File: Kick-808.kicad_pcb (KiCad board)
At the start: 2 copper layers, 0 parts

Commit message: PCB layout preparation.
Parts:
- added Accent1: AudioJack2_SwitchT, Local:PJ398SM, F.Cu at (197.0, 93.5)
- added C1: 100n, Capacitor_SMD:C_0603_1608Metric, F.Cu at (225.6, 79.8)
- added C10: 15n, Capacitor_SMD:C_0603_1608Metric, F.Cu at (214.2, 91.6)
- added C11: 22n, Capacitor_SMD:C_0603_1608Metric, F.Cu at (208.5, 93.9)
- added C12: 1u, Capacitor_SMD:C_0603_1608Metric, F.Cu at (204.0, 98.5)
- added C13: 10u, Capacitor_SMD:CP_Elec_4x5.8, F.Cu at (217.3, 74.4)
- added C2: 100n, Capacitor_SMD:C_0603_1608Metric, F.Cu at (219.8, 83.1)
- added C3: 22u, Capacitor_SMD:CP_Elec_5x5.4, F.Cu at (207.7, 89.2)
- added C4: 22u, Capacitor_SMD:CP_Elec_5x5.4, F.Cu at (179.0, 105.1)
- added C5: 15n, Capacitor_SMD:C_0603_1608Metric, F.Cu at (225.6, 77.3)
- added C6: 100n, Capacitor_SMD:C_0603_1608Metric, F.Cu at (172.7, 109.8)
- added C7: 100n, Capacitor_SMD:C_0603_1608Metric, F.Cu at (204.0, 101.0)
- added C8: 33n, Capacitor_SMD:C_0603_1608Metric, F.Cu at (216.5, 94.1)
- added C9: 15n, Capacitor_SMD:C_0603_1608Metric, F.Cu at (208.5, 96.4)
- added D1: 1N4148, Diode_SMD:D_SOD-123, F.Cu at (186.4, 109.6)
- added D2: 1N4148, Diode_SMD:D_SOD-123, F.Cu at (224.0, 73.1)
- added D3: 1N4148, Diode_SMD:D_SOD-123, F.Cu at (216.3, 79.0)
- added Decay1: 100k, Local:AlpsRK09K, F.Cu at (167.3, 77.6)
- added FB1: Ferrite_Bead, Inductor_SMD:L_0603_1608Metric, F.Cu at (195.2, 107.1)
- added FB2: Ferrite_Bead, Inductor_SMD:L_0603_1608Metric, F.Cu at (218.6, 86.5)
- added J3: Conn_02x05_Odd_Even, Connector_PinHeader_2.54mm:PinHeader_2x05_P2.54mm_Vertical, F.Cu at (176.9, 89.2)
- added Mod1: 10k, Local:AlpsRK09K, F.Cu at (196.0, 77.6)
- added Mod2: 100k, Local:AlpsRK09K, F.Cu at (181.7, 77.6)
- added Output1: AudioJack2_SwitchT, Local:PJ398SM, F.Cu at (208.3, 78.0)
- added Q1: BC847, Package_TO_SOT_SMD:SOT-23, F.Cu at (204.3, 94.9)
- added Q2: BC847, Package_TO_SOT_SMD:SOT-23, F.Cu at (215.6, 82.9)
- added Q3: BC857, Package_TO_SOT_SMD:SOT-23, F.Cu at (194.7, 103.5)
- added Q4: BC847, Package_TO_SOT_SMD:SOT-23, F.Cu at (214.4, 88.1)
- added Q5: BC847, Package_TO_SOT_SMD:SOT-23, F.Cu at (221.4, 79.6)
- added Q6: BC847, Package_TO_SOT_SMD:SOT-23, F.Cu at (199.1, 103.5)
- added Q7: BC847, Package_TO_SOT_SMD:SOT-23, F.Cu at (229.1, 73.7)
- added R1: 2k2, Resistor_SMD:R_0603_1608Metric, F.Cu at (191.2, 109.2)
- added R10: 10k, Resistor_SMD:R_0603_1608Metric, F.Cu at (203.3, 106.0)
- added R11: 100k, Resistor_SMD:R_0603_1608Metric, F.Cu at (226.2, 90.6)
- added R12: 1M, Resistor_SMD:R_0603_1608Metric, F.Cu at (218.2, 91.6)
- added R13: 4k7, Resistor_SMD:R_0603_1608Metric, F.Cu at (208.0, 98.9)
- added R14: 10k, Resistor_SMD:R_0603_1608Metric, F.Cu at (203.3, 103.5)
- added R15: 22k, Resistor_SMD:R_0603_1608Metric, F.Cu at (229.6, 77.3)
- added R16: 100k, Resistor_SMD:R_0603_1608Metric, F.Cu at (218.6, 89.0)
- added R17: 4k7, Resistor_SMD:R_0603_1608Metric, F.Cu at (225.6, 82.3)
- added R18: 100k, Resistor_SMD:R_0603_1608Metric, F.Cu at (212.5, 94.1)
- added R19: 1M, Resistor_SMD:R_0603_1608Metric, F.Cu at (199.3, 107.1)
- added R2: 1k5, Resistor_SMD:R_0603_1608Metric, F.Cu at (180.8, 109.8)
- added R20: 1M, Resistor_SMD:R_0603_1608Metric, F.Cu at (208.0, 101.4)
- added R21: 1k, Resistor_SMD:R_0603_1608Metric, F.Cu at (176.7, 109.8)
- added R22: 220, Resistor_SMD:R_0603_1608Metric, F.Cu at (216.1, 99.1)
- added R23: 100k, Resistor_SMD:R_0603_1608Metric, F.Cu at (226.7, 87.3)
- added R24: 470k, Resistor_SMD:R_0603_1608Metric, F.Cu at (220.5, 94.1)
- added R25: 10k, Resistor_SMD:R_0603_1608Metric, F.Cu at (216.5, 96.6)
- added R26: 100k, Resistor_SMD:R_0603_1608Metric, F.Cu at (212.1, 101.6)
- added R27: 4k7, Resistor_SMD:R_0603_1608Metric, F.Cu at (207.3, 106.5)
- added R28: 1k, Resistor_SMD:R_0603_1608Metric, F.Cu at (222.6, 88.1)
- added R29: 10k, Resistor_SMD:R_0603_1608Metric, F.Cu at (207.3, 103.9)
- added R3: 200k, Resistor_SMD:R_0603_1608Metric, F.Cu at (222.2, 91.5)
- added R30: 680, Resistor_SMD:R_0603_1608Metric, F.Cu at (226.7, 84.8)
- added R31: 47k, Resistor_SMD:R_0603_1608Metric, F.Cu at (203.3, 108.5)
- added R32: 1k, Resistor_SMD:R_0603_1608Metric, F.Cu at (212.1, 99.1)
- added R4: 47k, Resistor_SMD:R_0603_1608Metric, F.Cu at (229.6, 82.3)
- added R5: 100k, Resistor_SMD:R_0603_1608Metric, F.Cu at (195.2, 109.6)
- added R6: 100k, Resistor_SMD:R_0603_1608Metric, F.Cu at (222.6, 85.6)
- added R7: 8k2, Resistor_SMD:R_0603_1608Metric, F.Cu at (199.3, 109.6)
- added R8: 2k7, Resistor_SMD:R_0603_1608Metric, F.Cu at (212.5, 96.6)
- added R9: 22k, Resistor_SMD:R_0603_1608Metric, F.Cu at (229.6, 79.8)
- added SW1: SW_Push_LED, Local:SW_PUSH_LED_6mm, F.Cu at (165.4, 106.7)
- added Tone1: 100k, Local:AlpsRK09K, F.Cu at (167.3, 93.1)
- added Trigger1: AudioJack2_SwitchT, Local:PJ398SM, F.Cu at (186.8, 93.5)
- added U1: TL074, Package_SO:TSSOP-14_4.4x5mm_P0.65mm, F.Cu at (188.0, 104.6)
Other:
- board outline added: 19.3 x 106.5 mm

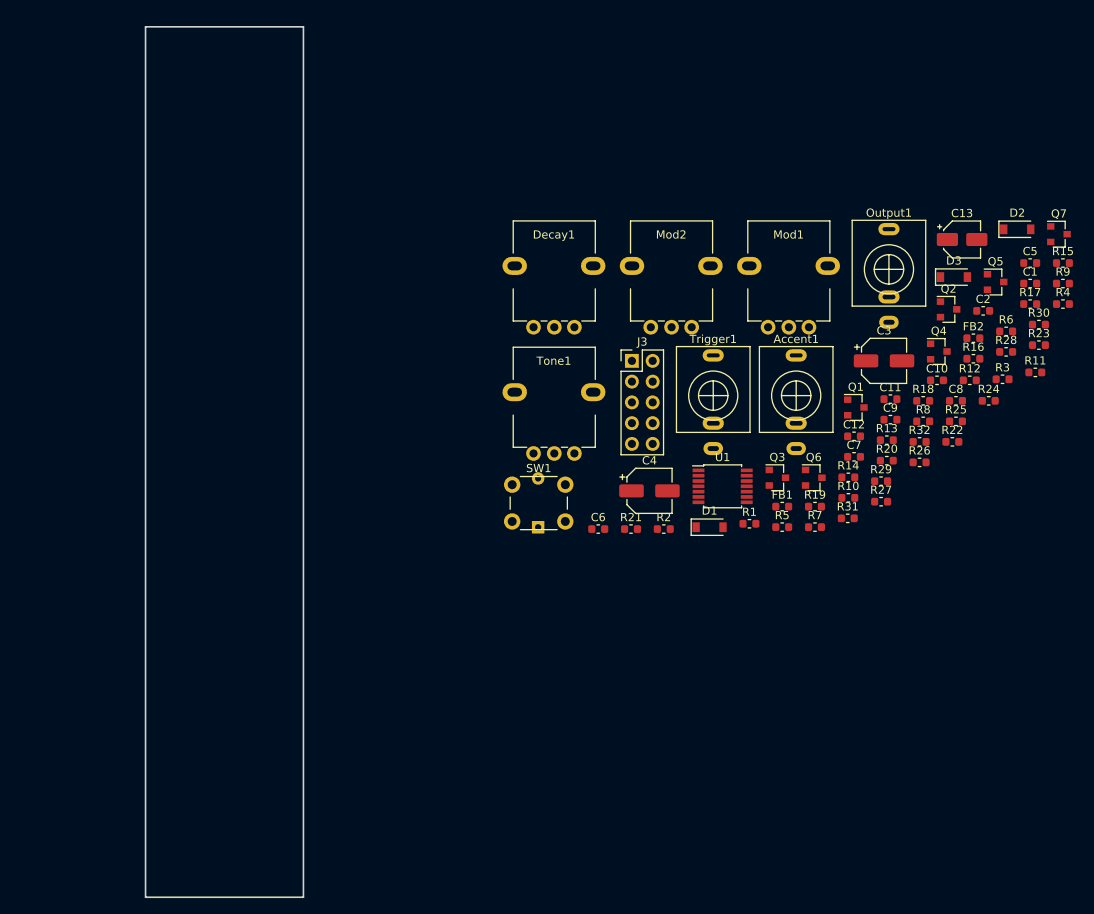
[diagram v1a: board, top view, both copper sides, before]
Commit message: Use SMD pin header and get ready for placement.
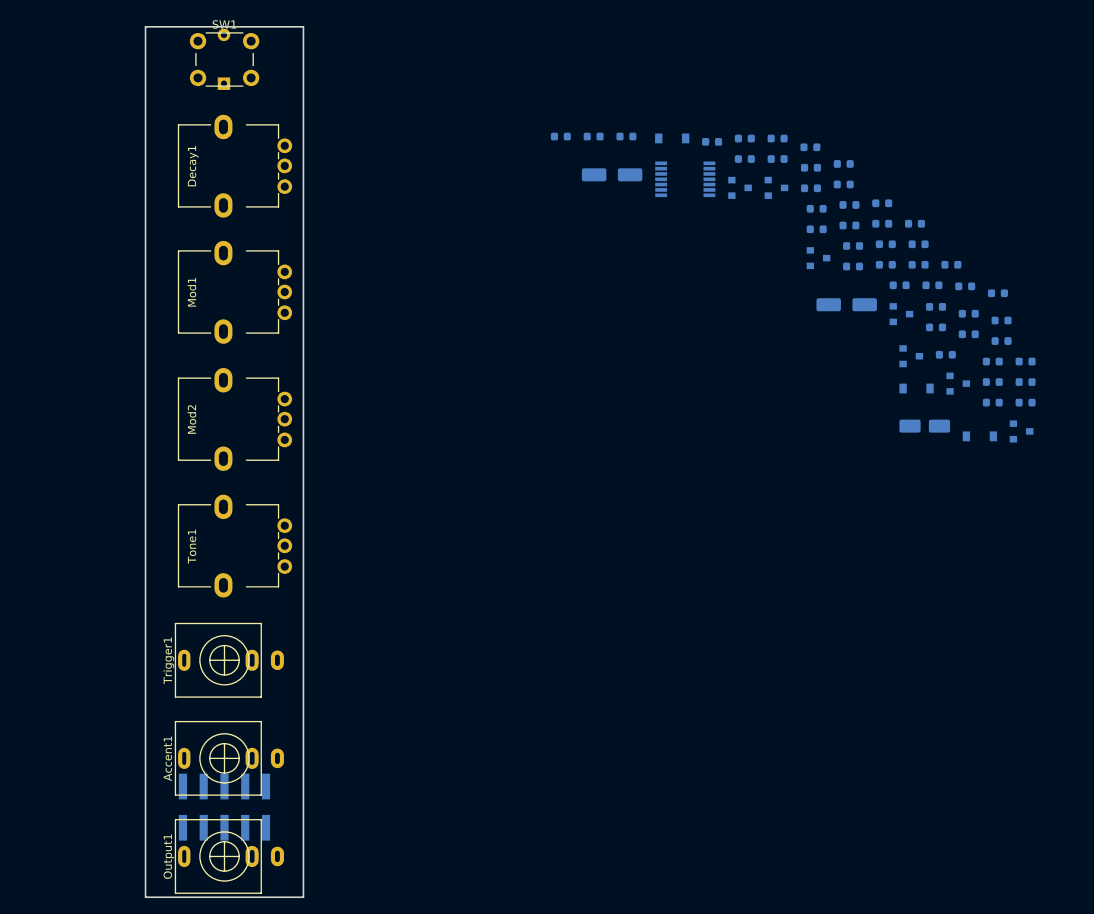
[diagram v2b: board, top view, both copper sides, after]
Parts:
- C1, C10, C11, C12, C13, C2, C3, C4, C5, C6, C7, C8, C9, D1, D2, D3, FB1, FB2, Q1, Q2, Q3, Q4, Q5, Q6, Q7, R1, R10, R11, R12, R13, R14, R15, R16, R17, R18, R19, R2, R20, R21, R22, R23, R24, R25, R26, R27, R28, R29, R3, R30, R31, R32, R4, R5, R6, R7, R8, R9, U1: moved to B.Cu
- J3: footprint Connector_PinHeader_2.54mm:PinHeader_2x05_P2.54mm_Vertical -> Connector_PinHeader_2.54mm:PinHeader_2x05_P2.54mm_Vertical_SMD; moved to B.Cu
- moved Output1 108.5 mm to (127.0, 149.9), turned to 90 degrees
- moved Accent1 82.8 mm to (127.0, 137.9), turned to 90 degrees
- moved J3 73.9 mm to (127.0, 143.8), turned to 90 degrees
- moved Mod1 69.2 mm to (126.9, 80.8), turned to 90 degrees
- moved Trigger1 68.0 mm to (127.0, 125.9), turned to 90 degrees
- moved SW1 66.5 mm to (126.9, 52.4)
- moved Mod2 57.9 mm to (126.9, 96.4), turned to 90 degrees
- moved C6 48.2 mm to (168.2, 61.8)
- moved R2 48.2 mm to (176.2, 61.8)
- moved R21 48.2 mm to (172.2, 61.8)
- moved D1 47.8 mm to (181.8, 62.0)
- moved R5 47.8 mm to (190.7, 62.0)
- moved R7 47.8 mm to (194.7, 62.0)
- moved R1 47.0 mm to (186.7, 62.4)
- moved R31 45.6 mm to (198.7, 63.1)
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
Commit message: Use 2 dual op-amps for better layout.
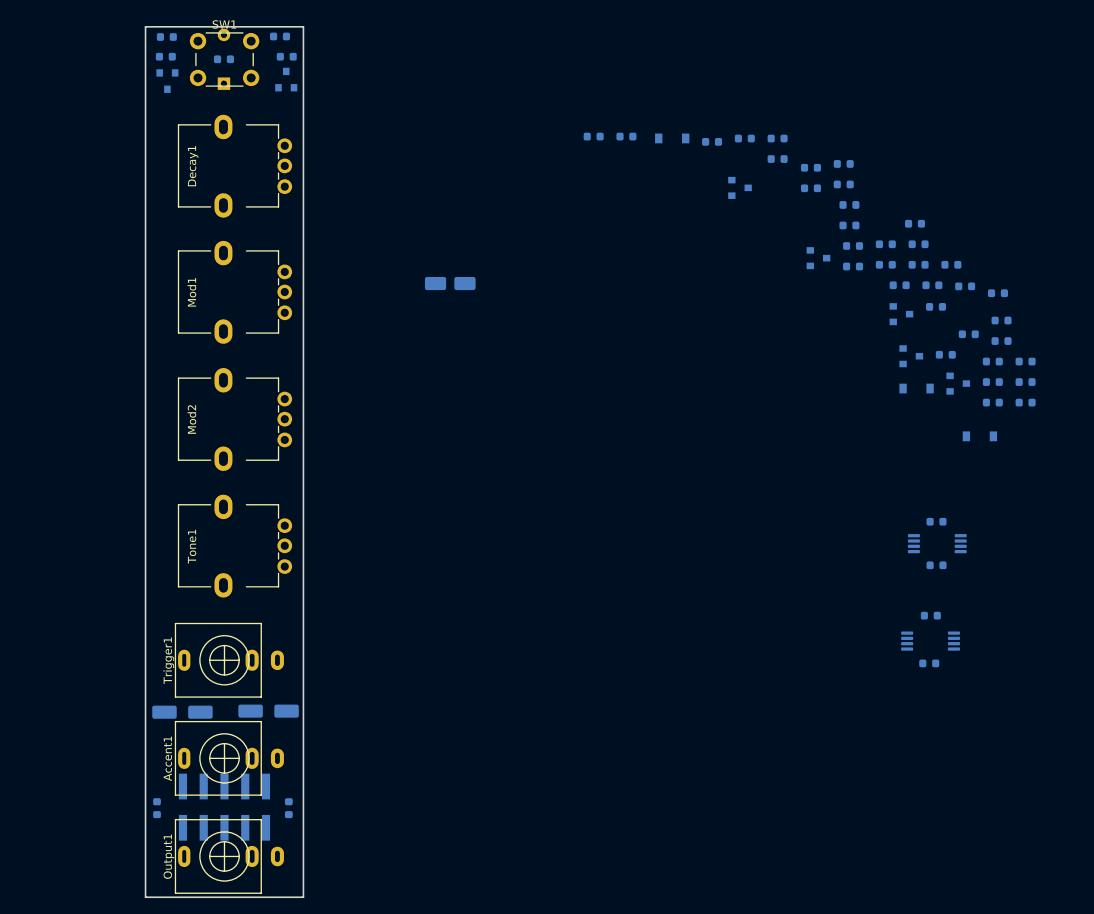
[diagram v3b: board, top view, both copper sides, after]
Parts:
- added C14: 100n, Capacitor_SMD:C_0603_1608Metric, B.Cu at (213.2, 126.2)
- added C15: 100n, Capacitor_SMD:C_0603_1608Metric, B.Cu at (213.4, 120.4)
- added U2: TL072, Package_SO:TSSOP-8_4.4x3mm_P0.65mm, B.Cu at (214.2, 111.6)
- U1: value TL074 -> TL072; footprint Package_SO:TSSOP-14_4.4x5mm_P0.65mm -> Package_SO:TSSOP-8_4.4x3mm_P0.65mm
- moved Q7 113.0 mm to (120.0, 55.0), turned to 270 degrees
- moved FB1 107.2 mm to (118.7, 144.0), turned to 270 degrees
- moved FB2 98.6 mm to (134.9, 144.0), turned to 270 degrees
- moved C3 95.3 mm to (121.9, 132.2)
- moved R28 90.8 mm to (133.8, 49.5)
- moved R32 90.5 mm to (120.0, 49.6)
- moved R31 79.6 mm to (119.8, 52.0)
- moved C4 77.9 mm to (132.4, 132.1)
- moved C12 75.4 mm to (126.9, 52.3)
- moved R26 75.0 mm to (134.6, 52.0), turned to 180 degrees
- moved C6 69.7 mm to (214.1, 114.2)
- moved U1 64.0 mm to (213.4, 123.5)
- moved Q6 61.4 mm to (134.6, 54.8), turned to 90 degrees
- moved C13 60.6 mm to (154.6, 79.8)
- moved C7 41.0 mm to (214.1, 108.9)
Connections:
- U1 pad 1: Net-(C10-Pad1) -> Net-(Q3-Pad2)
- U1 pad 2: Net-(C9-Pad2) -> Net-(R11-Pad2)
- U1 pad 3: Net-(C5-Pad1) -> Net-(R3-Pad1)
- U1 pad 4: +12V -> -12V
- U1 pad 5: Net-(R27-Pad1) -> Net-(C11-Pad1)
- U1 pad 6: Net-(Decay1-Pad1) -> Net-(R30-Pad2)
- U1 pad 7: Net-(C13-Pad2) -> Net-(R30-Pad2)
- U1 pad 8: Net-(R30-Pad2) -> +12V

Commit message: Outline placement.
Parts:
- moved R15 119.8 mm to (107.4, 71.2), turned to 180 degrees
- moved R30 118.4 mm to (108.1, 119.0)
- moved R4 117.6 mm to (107.7, 98.3), turned to 180 degrees
- moved R11 116.5 mm to (107.7, 105.3)
- moved D2 113.9 mm to (107.5, 77.4)
- moved C2 111.0 mm to (107.3, 63.0), turned to 180 degrees
- moved R3 110.7 mm to (108.0, 95.2), turned to 180 degrees
- moved C14 108.9 mm to (105.3, 112.0), turned to 270 degrees
- moved R12 108.2 mm to (107.3, 60.2)
- moved U1 106.0 mm to (108.0, 112.1), turned to 270 degrees
- moved C11 105.5 mm to (108.3, 122.1), turned to 180 degrees
- moved C8 104.5 mm to (107.5, 74.2), turned to 180 degrees
- moved Q4 103.7 mm to (107.4, 67.2), turned to 180 degrees
- moved R8 103.1 mm to (107.1, 53.2), turned to 180 degrees
- moved C15 102.6 mm to (111.1, 112.1), turned to 270 degrees
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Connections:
- Accent1 pad S: GND -> (no net)
- C11 pad 2: GND -> (no net)
- C12 pad 2: GND -> (no net)
- C14 pad 1: GND -> (no net)
- C15 pad 2: GND -> (no net)
- C2 pad 2: GND -> (no net)
- C3 pad 2: GND -> (no net)
- C4 pad 1: GND -> (no net)
- C6 pad 1: GND -> (no net)
- C7 pad 2: GND -> (no net)
- D2 pad 1: GND -> (no net)
- D3 pad 2: GND -> (no net)
- J3 pad 3: GND -> (no net)
- J3 pad 4: GND -> (no net)
- J3 pad 5: GND -> (no net)
- J3 pad 6: GND -> (no net)
- J3 pad 7: GND -> (no net)
- J3 pad 8: GND -> (no net)
- Mod2 pad 2: GND -> (no net)
- Mod2 pad 3: GND -> (no net)
- Output1 pad S: GND -> (no net)
- Q1 pad 2: GND -> (no net)
- Q2 pad 2: GND -> (no net)
- Q4 pad 2: GND -> (no net)
- Q5 pad 2: GND -> (no net)
- Q7 pad 2: GND -> (no net)
- R10 pad 2: GND -> (no net)
- R17 pad 2: GND -> (no net)
- R2 pad 2: GND -> (no net)
- R27 pad 2: GND -> (no net)
- R5 pad 2: GND -> (no net)
- R6 pad 2: GND -> (no net)
- R8 pad 1: GND -> (no net)
- Trigger1 pad S: GND -> (no net)

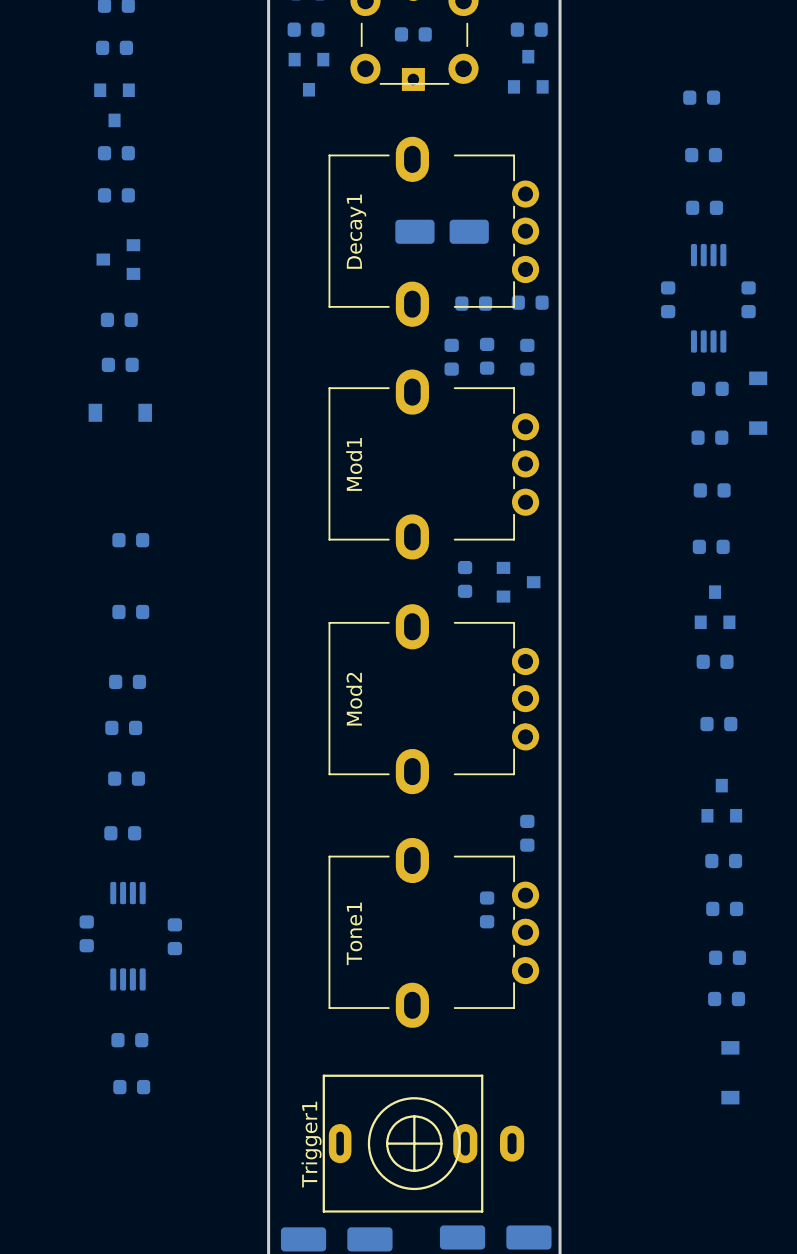
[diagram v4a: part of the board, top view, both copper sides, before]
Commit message: Initial placement on rear left-side.
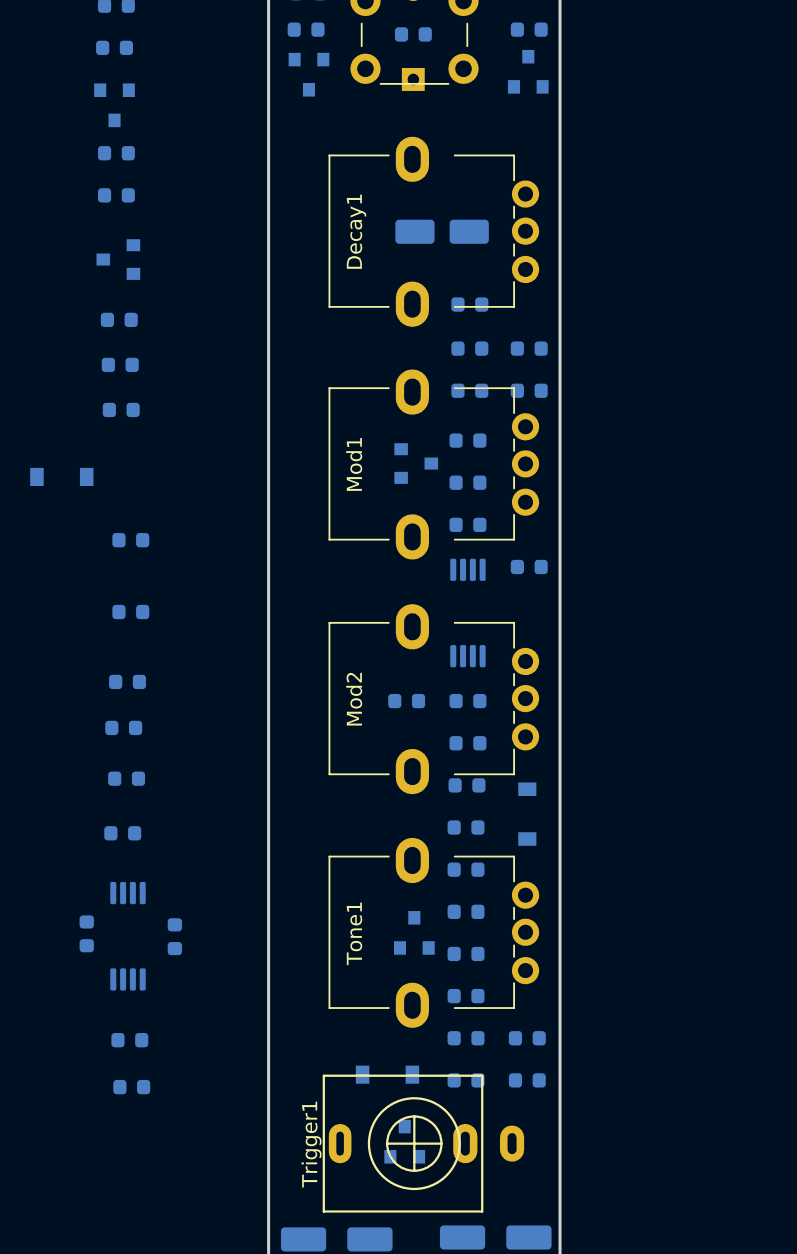
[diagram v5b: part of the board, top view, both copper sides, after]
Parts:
- moved C7 31.8 mm to (126.5, 96.5), turned to 180 degrees
- moved D3 31.2 mm to (134.5, 104.0)
- moved Q2 30.9 mm to (126.4, 125.7)
- moved Q3 29.4 mm to (127.0, 111.9)
- moved R25 27.5 mm to (130.6, 79.2)
- moved R27 26.8 mm to (130.6, 82.0)
- moved U2 26.3 mm to (130.6, 90.7)
- moved R29 26.2 mm to (130.6, 84.8)
- moved R20 26.2 mm to (130.6, 96.5)
- moved R17 25.8 mm to (130.6, 99.3)
- moved R16 25.4 mm to (130.5, 102.1)
- moved R18 25.4 mm to (107.6, 77.2), turned to 180 degrees
- moved C5 24.7 mm to (130.4, 104.9)
- moved C6 22.9 mm to (134.6, 87.6), turned to 180 degrees
- moved D1 22.7 mm to (125.2, 121.3), turned to 180 degrees
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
